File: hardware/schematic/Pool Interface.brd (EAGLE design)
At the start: 63 x 58 mm, 11 parts, among them J2 RS485-TERM-SPTAF, J6 ESP-JTAG-2X05, U1 MAX3485CSA+

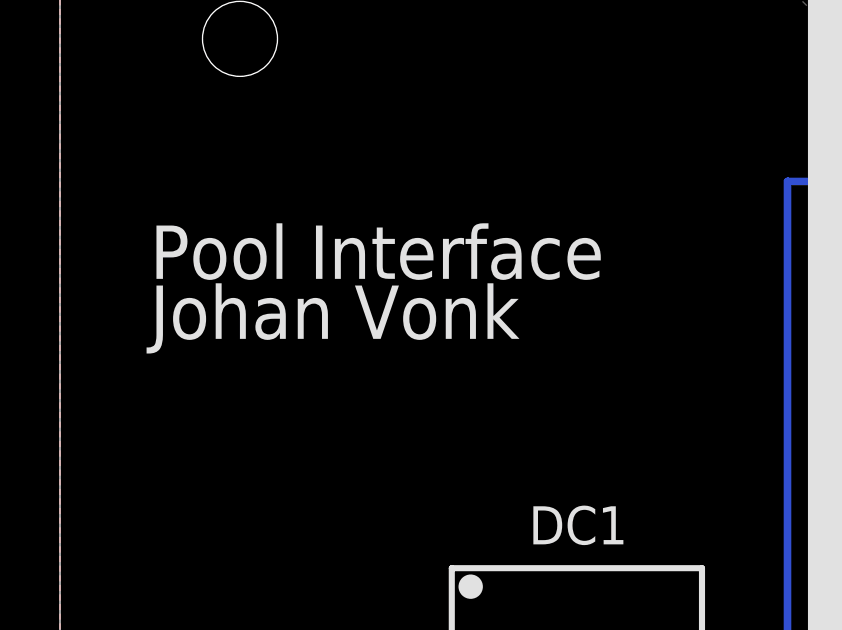
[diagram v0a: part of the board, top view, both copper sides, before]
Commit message: Schematic and board to SVG
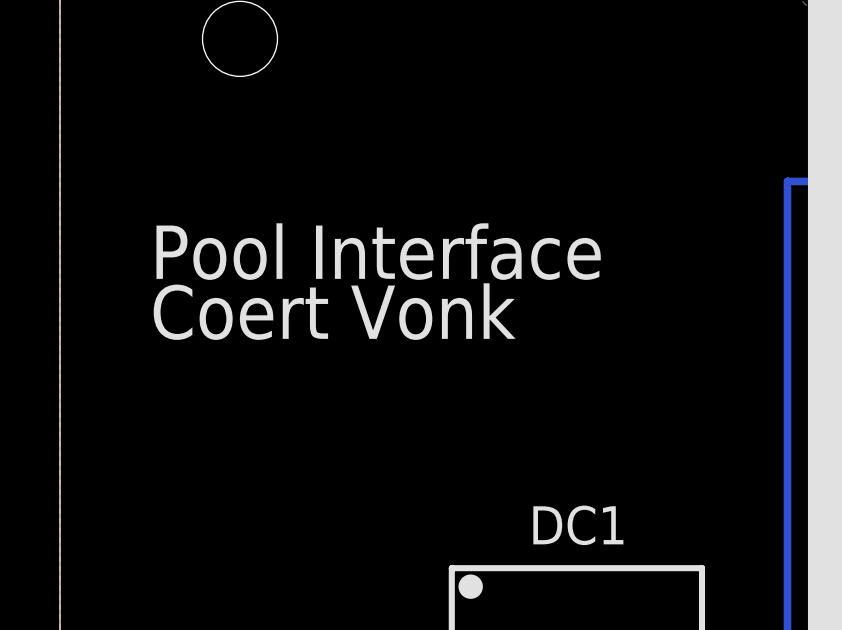
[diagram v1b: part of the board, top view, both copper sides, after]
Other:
- board text added: "Coert Vonk"
- board text removed: ">AUTHOR_NAME"
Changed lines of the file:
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@@
 <?xml version="1.0" encoding="utf-8"?>
 <!DOCTYPE eagle SYSTEM "eagle.dtd">
-<eagle version="9.4.0">
+<eagle version="9.6.2">
 <drawing>
 <settings>
@@
 <rectangle x1="29" y1="50" x2="47" y2="58" layer="41"/>
 <rectangle x1="29" y1="50" x2="47" y2="58" layer="42"/>
-<text x="3" y="42" size="1.778" layer="25">&gt;AUTHOR_NAME</text>
-<text x="31" y="36" size="1.778" layer="26" rot="MR180">&gt;AUTHOR_NAME</text>
+<text x="3" y="42" size="1.778" layer="25">Coert Vonk</text>
+<text x="31" y="36" size="1.778" layer="26" rot="MR180">Coert Vonk</text>
 </plain>
 <attributes>
